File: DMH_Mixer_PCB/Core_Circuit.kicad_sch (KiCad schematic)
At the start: 28 parts, among them SW1 SW_SPDT_321, SW2 SW_SPDT_321, SW3 SW_SPDT_321, SW4 SW_SPDT_321, U1 TL074

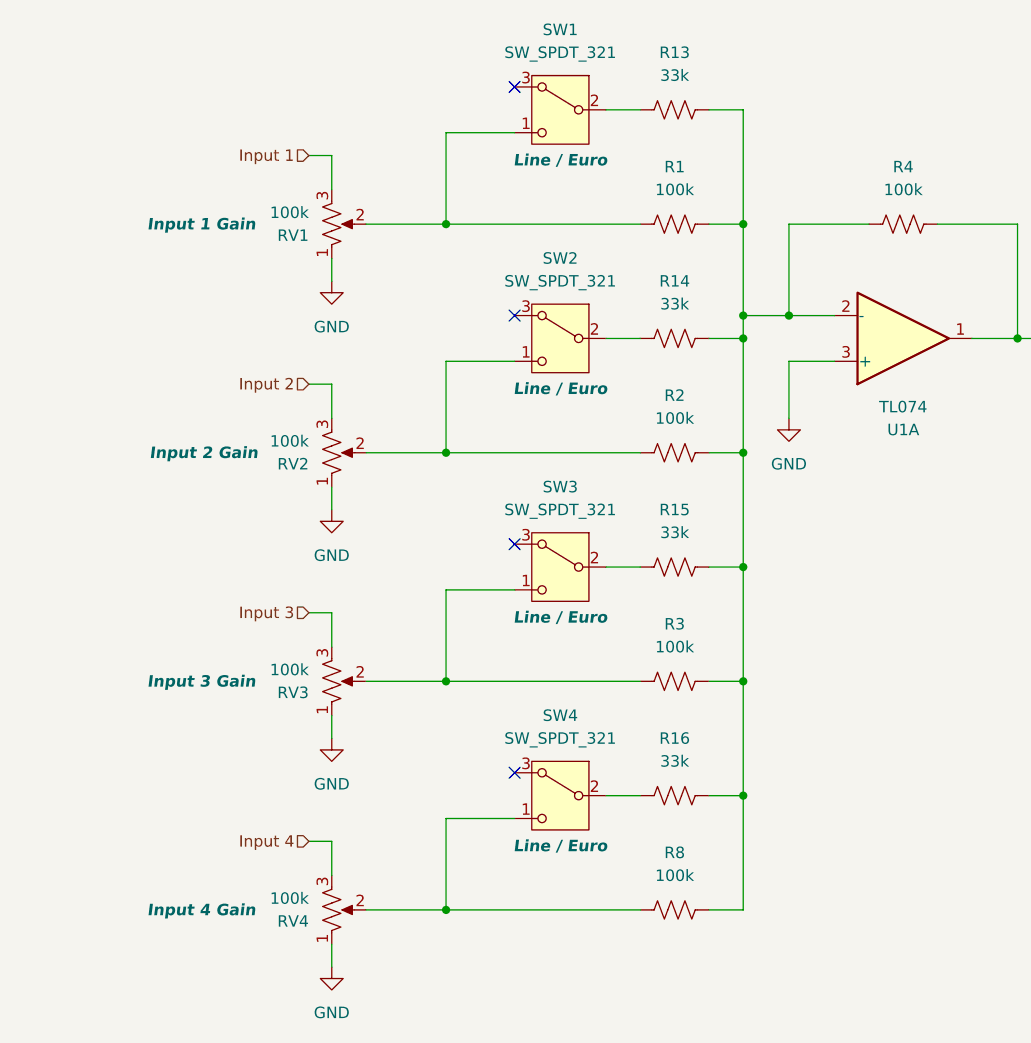
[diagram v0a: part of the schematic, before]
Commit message: Added AC coupling
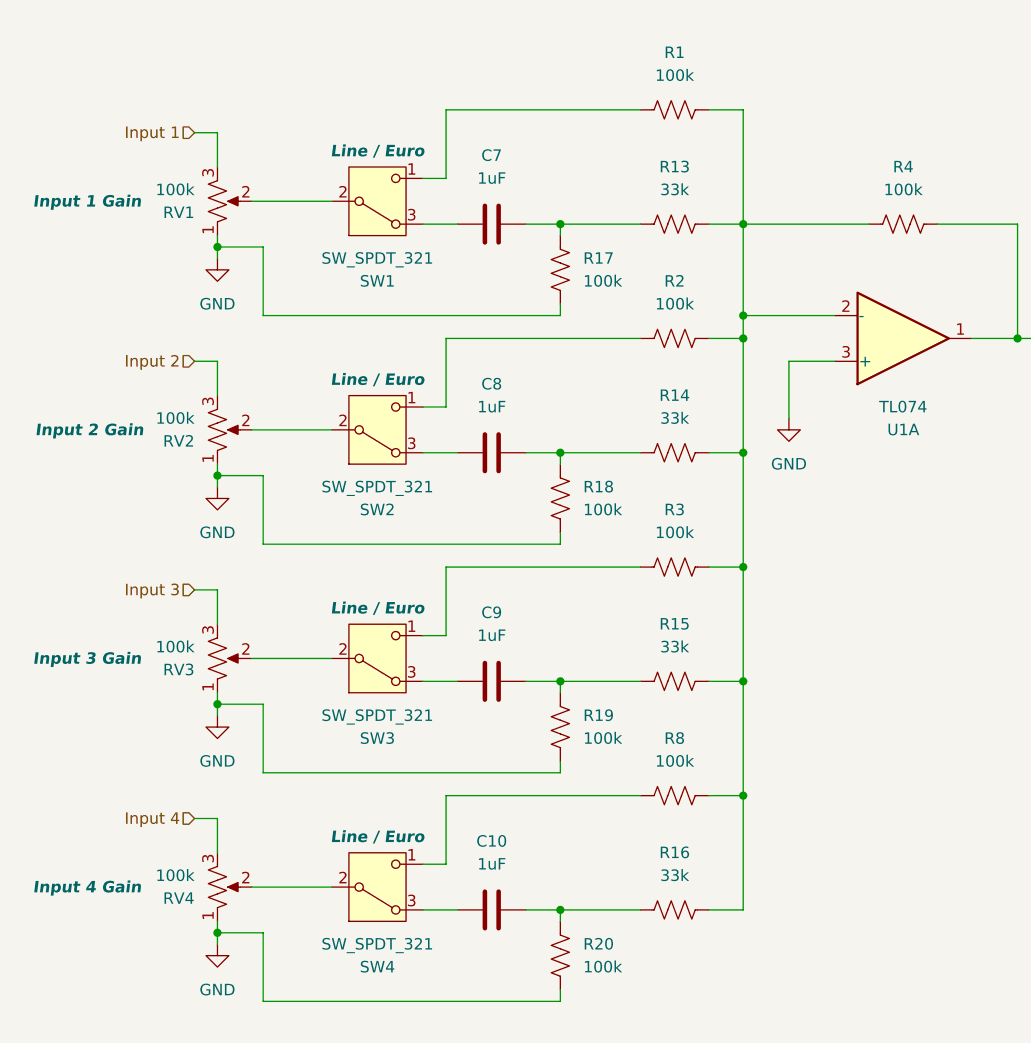
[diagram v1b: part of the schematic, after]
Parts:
- added C10, C7, C8, C9: 1uF, Capacitor_THT:C_Disc_D4.3mm_W1.9mm_P5.00mm, symbol Device:C
- added R17, R18, R19, R20: 100k, Resistor_THT:R_Axial_DIN0207_L6.3mm_D2.5mm_P7.62mm_Horizontal, symbol Device:R_US
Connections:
- net GND: now also R17.1, R18.1, R19.1, R20.1
- net at R14.1: now also C8.2, R18.2; no longer SW2.2 (B)
- net at R2.1, SW2.1 (C): no longer RV2.2
- net at R3.1, SW3.1 (C): no longer RV3.2
- net at R15.1: now also C9.2, R19.2; no longer SW3.2 (B)
- net at SW3.3 (A): now also C9.1
- net at R8.1, SW4.1 (C): no longer RV4.2
- net at R1.1, SW1.1 (C): no longer RV1.2
- net at SW2.3 (A): now also C8.1
- net at R13.1: now also C7.2, R17.2; no longer SW1.2 (B)
- net at R16.1: now also C10.2, R20.2; no longer SW4.2 (B)
- net at SW1.3 (A): now also C7.1
- net at SW4.3 (A): now also C10.1
- new net: RV3.2, SW3.2 (B)
- new net: RV1.2, SW1.2 (B)
- new net: RV2.2, SW2.2 (B)
- new net: RV4.2, SW4.2 (B)
- no-connect marks 4 -> 0
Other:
- moved on the sheet: R1, R13, R14, R15, R16, R2, R3, R8, RV1, RV2, RV3, RV4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

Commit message: Component placement done
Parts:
- R2: renamed from R13; value 33k -> 27k
- R4: renamed from R14; value 33k -> 27k
- R6: renamed from R15; value 33k -> 27k
- R8: renamed from R16; value 33k -> 27k
- renumbered R18 to R10, R19 to R11, R20 to R12, R4 to R13, R5 to R14, R6 to R15, R7 to R16, R9 to R17, R11 to R18, R10 to R19, R12 to R20, R2 to R3, R3 to R5, R8 to R7, R17 to R9
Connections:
- net at C7.1: now also SW1.1 (C); no longer SW1.3 (A)
- net at R3.1: now also SW2.3 (A); no longer SW2.1 (C)
- net at SW3.1 (C): now also C9.1; no longer R5.1
- net at SW3.3 (A): now also R5.1; no longer C9.1
- net at C8.1: now also SW2.1 (C); no longer SW2.3 (A)
- net at R7.1: now also SW4.3 (A); no longer SW4.1 (C)
- net at R1.1: now also SW1.3 (A); no longer SW1.1 (C)
- net at C10.1: now also SW4.1 (C); no longer SW4.3 (A)
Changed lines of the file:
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@@
 		(dnp no)
 		(fields_autoplaced yes)
-		(property "Reference" "R14"
+		(property "Reference" "R4"
 			(at 88.9 82.55 90)
 			(effects
@@
 			)
 		)
-		(property "Value" "33k"
+		(property "Value" "27k"
 			(at 88.9 85.09 90)
 			(effects
@@
 			(project "DMH_Mixer_PCB"
 				(path "/58f4306d-5387-4983-bb08-41a2313fd315/7ad2d702-dfb7-4d49-a82d-34430dd5948f"
-					(reference "R14")
+					(reference "R4")
 					(unit 1)
 				)
@@
 		(dnp no)
 		(fields_autoplaced yes)
-		(property "Reference" "R12"
+		(property "Reference" "R20"
 			(at 241.3 97.79 90)
 			(effects
@@
 			(project "DMH_Mixer_PCB"
 				(path "/58f4306d-5387-4983-bb08-41a2313fd315/7ad2d702-dfb7-4d49-a82d-34430dd5948f"
-					(reference "R12")
+					(reference "R20")
 					(unit 1)
 				)
@@
 		(dnp no)
 		(fields_autoplaced yes)
-		(property "Reference" "R19"
+		(property "Reference" "R11"
 			(at 78.74 118.1099 0)
 			(effects
@@
 			(project "DMH_Mixer_PCB"
 				(path "/58f4306d-5387-4983-bb08-41a2313fd315/7ad2d702-dfb7-4d49-a82d-34430dd5948f"
-					(reference "R19")
+					(reference "R11")
 					(unit 1)
 				)
@@
 		(dnp no)
 		(fields_autoplaced yes)
-		(property "Reference" "R9"
+		(property "Reference" "R17"
 			(at 171.45 95.25 90)
 			(effects
@@
 			(project "DMH_Mixer_PCB"
 				(path "/58f4306d-5387-4983-bb08-41a2313fd315/7ad2d702-dfb7-4d49-a82d-34430dd5948f"
-					(reference "R9")
+					(reference "R17")
 					(unit 1)
 				)
@@
 		(dnp no)
 		(fields_autoplaced yes)
-		(property "Reference" "R2"
+		(property "Reference" "R3"
 			(at 88.9 69.85 90)
 			(effects
@@
 			(project "DMH_Mixer_PCB"
 				(path "/58f4306d-5387-4983-bb08-41a2313fd315/7ad2d702-dfb7-4d49-a82d-34430dd5948f"
-					(reference "R2")
+					(reference "R3")
 					(unit 1)
 				)
@@
 		(lib_id "Switch:SW_SPDT_321")
 		(at 55.88 111.76 0)
-		(mirror x)
 		(unit 1)
 		(exclude_from_sim no)
@@
 		(dnp no)
 		(property "Reference" "SW3"
-			(at 55.88 120.65 0)
+			(at 55.88 102.87 0)
 			(effects
 				(font
@@
 		)
 		(property "Value" "SW_SPDT_321"
-			(at 55.88 118.11 0)
+			(at 55.88 105.41 0)
 			(effects
 				(font
@@
 		)
 		(property "Footprint" "SynthStuff:Toggle_Switch_THT"
-			(at 55.88 101.6 0)
+			(at 55.88 121.92 0)
 			(effects
 				(font
@@
 		)
 		(property "Datasheet" "~"
-			(at 55.88 104.14 0)
+			(at 55.88 119.38 0)
 			(effects
 				(font
@@
 		)
 		(property "Function" "Line / Euro"
-			(at 55.88 106.172 0)
+			(at 55.88 117.348 0)
 			(effects
 				(font
@@
 		(dnp no)
 		(fields_autoplaced yes)
-		(property "Reference" "R8"
+		(property "Reference" "R7"
 			(at 88.9 120.65 90)
 			(effects
@@
 			(project "DMH_Mixer_PCB"
 				(path "/58f4306d-5387-4983-bb08-41a2313fd315/7ad2d702-dfb7-4d49-a82d-34430dd5948f"
-					(reference "R8")
+					(reference "R7")
 					(unit 1)
 				)
@@
 		(dnp no)
 		(fields_autoplaced yes)
-		(property "Reference" "R17"
+		(property "Reference" "R9"
 			(at 78.74 67.3099 0)
 			(effects
@@
 			(project "DMH_Mixer_PCB"
 				(path "/58f4306d-5387-4983-bb08-41a2313fd315/7ad2d702-dfb7-4d49-a82d-34430dd5948f"
-					(reference "R17")
+					(reference "R9")
 					(unit 1)
 				)
@@
 		(dnp no)
 		(fields_autoplaced yes)
-		(property "Reference" "R20"
+		(property "Reference" "R12"
 			(at 78.74 143.5099 0)
 			(effects
@@
 			(project "DMH_Mixer_PCB"
 				(path "/58f4306d-5387-4983-bb08-41a2313fd315/7ad2d702-dfb7-4d49-a82d-34430dd5948f"
-					(reference "R20")
+					(reference "R12")
 					(unit 1)
 				)
@@
 		(dnp no)
 		(fields_autoplaced yes)
-		(property "Reference" "R3"
+		(property "Reference" "R5"
 			(at 88.9 95.25 90)
 			(effects
@@
 			(project "DMH_Mixer_PCB"
 				(path "/58f4306d-5387-4983-bb08-41a2313fd315/7ad2d702-dfb7-4d49-a82d-34430dd5948f"
-					(reference "R3")
+					(reference "R5")
 					(unit 1)
 				)
@@
 		(lib_id "Switch:SW_SPDT_321")
 		(at 55.88 86.36 0)
-		(mirror x)
 		(unit 1)
 		(exclude_from_sim no)
@@
 		(dnp no)
 		(property "Reference" "SW2"
-			(at 55.88 95.25 0)
+			(at 55.88 77.47 0)
 			(effects
 				(font
@@
 		)
 		(property "Value" "SW_SPDT_321"
-			(at 55.88 92.71 0)
+			(at 55.88 80.01 0)
 			(effects
 				(font
@@
 		)
 		(property "Footprint" "SynthStuff:Toggle_Switch_THT"
-			(at 55.88 76.2 0)
+			(at 55.88 96.52 0)
 			(effects
 				(font
@@
 		)
 		(property "Datasheet" "~"
-			(at 55.88 78.74 0)
+			(at 55.88 93.98 0)
 			(effects
 				(font
@@
 		)
 		(property "Function" "Line / Euro"
-			(at 55.88 80.772 0)
+			(at 55.88 91.948 0)
 			(effects
 				(font
@@
 		(dnp no)
 		(fields_autoplaced yes)
-		(property "Reference" "R7"
+		(property "Reference" "R16"
 			(at 215.9 74.93 90)
 			(effects
@@
 			(project "DMH_Mixer_PCB"
 				(path "/58f4306d-5387-4983-bb08-41a2313fd315/7ad2d702-dfb7-4d49-a82d-34430dd5948f"
-					(reference "R7")
+					(reference "R16")
 					(unit 1)
 				)
@@
 		(dnp no)
 		(fields_autoplaced yes)
-		(property "Reference" "R13"
+		(property "Reference" "R2"
 			(at 88.9 57.15 90)
 			(effects
@@
 			)
 		)
-		(property "Value" "33k"
+		(property "Value" "27k"
 			(at 88.9 59.69 90)
 			(effects
@@
 			(project "DMH_Mixer_PCB"
 				(path "/58f4306d-5387-4983-bb08-41a2313fd315/7ad2d702-dfb7-4d49-a82d-34430dd5948f"
-					(reference "R13")
+					(reference "R2")
 					(unit 1)
 				)
@@
 		(on_board yes)
 		(dnp no)
-		(property "Reference" "R10"
+		(property "Reference" "R19"
 			(at 215.9 120.65 90)
 			(effects
@@
 			(project "DMH_Mixer_PCB"
 				(path "/58f4306d-5387-4983-bb08-41a2313fd315/7ad2d702-dfb7-4d49-a82d-34430dd5948f"
-					(reference "R10")
+					(reference "R19")
 					(unit 1)
 				)
@@
 		(dnp no)
 		(fields_autoplaced yes)
-		(property "Reference" "R4"
+		(property "Reference" "R13"
 			(at 114.3 57.15 90)
 			(effects
@@
 			(project "DMH_Mixer_PCB"
 				(path "/58f4306d-5387-4983-bb08-41a2313fd315/7ad2d702-dfb7-4d49-a82d-34430dd5948f"
-					(reference "R4")
+					(reference "R13")
 					(unit 1)
 				)
@@
 		(dnp no)
 		(fields_autoplaced yes)
-		(property "Reference" "R15"
+		(property "Reference" "R6"
 			(at 88.9 107.95 90)
 			(effects
@@
 			)
 		)
-		(property "Value" "33k"
+		(property "Value" "27k"
 			(at 88.9 110.49 90)
 			(effects
@@
 			(project "DMH_Mixer_PCB"
 				(path "/58f4306d-5387-4983-bb08-41a2313fd315/7ad2d702-dfb7-4d49-a82d-34430dd5948f"
-					(reference "R15")
+					(reference "R6")
 					(unit 1)
 				)
@@
 		(dnp no)
 		(fields_autoplaced yes)
-		(property "Reference" "R16"
+		(property "Reference" "R8"
 			(at 88.9 133.35 90)
 			(effects
@@
 			)
 		)
-		(property "Value" "33k"
+		(property "Value" "27k"
 			(at 88.9 135.89 90)
 			(effects
@@
 			(project "DMH_Mixer_PCB"
 				(path "/58f4306d-5387-4983-bb08-41a2313fd315/7ad2d702-dfb7-4d49-a82d-34430dd5948f"
-					(reference "R16")
+					(reference "R8")
 					(unit 1)
 				)
@@
 		(dnp no)
 		(fields_autoplaced yes)
-		(property "Reference" "R18"
+		(property "Reference" "R10"
 			(at 78.74 92.7099 0)
 			(effects
@@
 			(project "DMH_Mixer_PCB"
 				(path "/58f4306d-5387-4983-bb08-41a2313fd315/7ad2d702-dfb7-4d49-a82d-34430dd5948f"
-					(reference "R18")
+					(reference "R10")
 					(unit 1)
 				)
@@
 		(lib_id "Switch:SW_SPDT_321")
 		(at 55.88 60.96 0)
-		(mirror x)
 		(unit 1)
 		(exclude_from_sim no)
@@
 		(dnp no)
 		(property "Reference" "SW1"
-			(at 55.88 69.85 0)
+			(at 55.88 52.07 0)
 			(effects
 				(font
@@
 		)
 		(property "Value" "SW_SPDT_321"
-			(at 55.88 67.31 0)
+			(at 55.88 54.61 0)
 			(effects
 				(font
@@
 		)
 		(property "Footprint" "SynthStuff:Toggle_Switch_THT"
-			(at 55.88 50.8 0)
+			(at 55.88 71.12 0)
 			(effects
 				(font
@@
 		)
 		(property "Datasheet" "~"
-			(at 55.88 53.34 0)
+			(at 55.88 68.58 0)
 			(effects
 				(font
@@
 		)
 		(property "Function" "Line / Euro"
-			(at 55.88 55.372 0)
+			(at 55.88 66.548 0)
 			(effects
 				(font
@@
 		(on_board yes)
 		(dnp no)
-		(property "Reference" "R11"
+		(property "Reference" "R18"
 			(at 200.66 119.3799 0)
 			(effects
@@
 			(project "DMH_Mixer_PCB"
 				(path "/58f4306d-5387-4983-bb08-41a2313fd315/7ad2d702-dfb7-4d49-a82d-34430dd5948f"
-					(reference "R11")
+					(reference "R18")
 					(unit 1)
 				)
@@
 		(dnp no)
 		(fields_autoplaced yes)
-		(property "Reference" "R6"
+		(property "Reference" "R15"
 			(at 152.4 57.15 90)
 			(effects
@@
 			(project "DMH_Mixer_PCB"
 				(path "/58f4306d-5387-4983-bb08-41a2313fd315/7ad2d702-dfb7-4d49-a82d-34430dd5948f"
-					(reference "R6")
+					(reference "R15")
 					(unit 1)
 				)
@@
 		(dnp no)
 		(fields_autoplaced yes)
-		(property "Reference" "R5"
+		(property "Reference" "R14"
 			(at 133.35 69.85 90)
 			(effects
@@
 			(project "DMH_Mixer_PCB"
 				(path "/58f4306d-5387-4983-bb08-41a2313fd315/7ad2d702-dfb7-4d49-a82d-34430dd5948f"
-					(reference "R5")
+					(reference "R14")
 					(unit 1)
 				)
@@
 		(lib_id "Switch:SW_SPDT_321")
 		(at 55.88 137.16 0)
-		(mirror x)
 		(unit 1)
 		(exclude_from_sim no)
@@
 		(dnp no)
 		(property "Reference" "SW4"
-			(at 55.88 146.05 0)
+			(at 55.88 128.27 0)
 			(effects
 				(font
@@
 		)
 		(property "Value" "SW_SPDT_321"
-			(at 55.88 143.51 0)
+			(at 55.88 130.81 0)
 			(effects
 				(font
@@
 		)
 		(property "Footprint" "SynthStuff:Toggle_Switch_THT"
-			(at 55.88 127 0)
+			(at 55.88 147.32 0)
 			(effects
 				(font
@@
 		)
 		(property "Datasheet" "~"
-			(at 55.88 129.54 0)
+			(at 55.88 144.78 0)
 			(effects
 				(font
@@
 		)
 		(property "Function" "Line / Euro"
-			(at 55.88 131.572 0)
+			(at 55.88 142.748 0)
 			(effects
 				(font

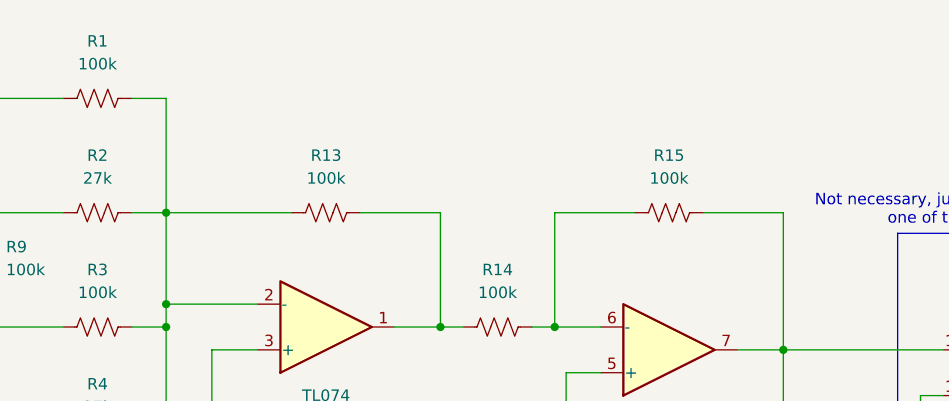
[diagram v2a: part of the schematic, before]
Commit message: ReRouted PCB
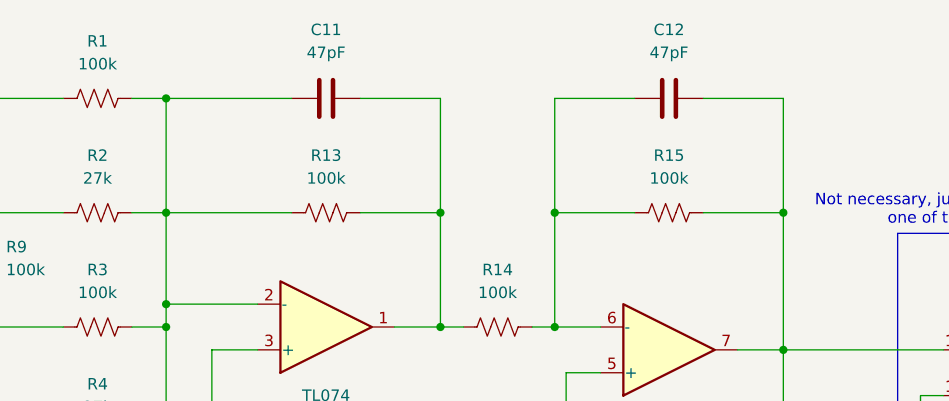
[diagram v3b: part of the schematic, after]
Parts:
- added C11, C12: 47pF, Capacitor_THT:C_Disc_D3.0mm_W2.0mm_P2.50mm, symbol Device:C
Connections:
- net at R1.2, R13.1, R2.2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: now also C11.1
- net at R15.2, R17.1, U1.12 (+)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: now also C12.2
- net at R13.2, R14.1, U1.1: now also C11.2
- net at R14.2, R15.1, U1.6 (-): now also C12.1
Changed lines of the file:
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@@
 	)
 	(junction
+		(at 165.1 63.5)
+		(diameter 0)
+		(color 0 0 0 0)
+	)
+	(junction
 		(at 38.1 142.24)
 		(diameter 0)
@@
 	)
 	(junction
+		(at 139.7 63.5)
+		(diameter 0)
+		(color 0 0 0 0)
+	)
+	(junction
 		(at 96.52 76.2)
 		(diameter 0)
@@
 	)
 	(junction
+		(at 127 63.5)
+		(diameter 0)
+		(color 0 0 0 0)
+	)
+	(junction
+		(at 96.52 50.8)
+		(diameter 0)
+		(color 0 0 0 0)
+	)
+	(junction
 		(at 190.5 101.6)
 		(diameter 0)
@@
 	(wire
 		(pts
+			(xy 148.59 50.8) (xy 139.7 50.8)
+		)
+		(stroke
+			(width 0)
+			(type default)
+		)
+	)
+	(wire
+		(pts
 			(xy 38.1 142.24) (xy 38.1 143.51)
 		)
@@
 	(wire
 		(pts
+			(xy 96.52 50.8) (xy 110.49 50.8)
+		)
+		(stroke
+			(width 0)
+			(type default)
+		)
+	)
+	(wire
+		(pts
 			(xy 223.52 104.14) (xy 228.6 104.14)
 		)
@@
 	(wire
 		(pts
+			(xy 139.7 50.8) (xy 139.7 63.5)
+		)
+		(stroke
+			(width 0)
+			(type default)
+		)
+	)
+	(wire
+		(pts
 			(xy 190.5 101.6) (xy 208.28 101.6)
 		)
@@
 	(wire
 		(pts
+			(xy 118.11 50.8) (xy 127 50.8)
+		)
+		(stroke
+			(width 0)
+			(type default)
+		)
+	)
+	(wire
+		(pts
 			(xy 76.2 73.66) (xy 76.2 72.39)
 		)
@@
 	(wire
 		(pts
+			(xy 165.1 50.8) (xy 165.1 63.5)
+		)
+		(stroke
+			(width 0)
+			(type default)
+		)
+	)
+	(wire
+		(pts
 			(xy 76.2 73.66) (xy 43.18 73.66)
 		)
@@
 	(wire
 		(pts
+			(xy 156.21 50.8) (xy 165.1 50.8)
+		)
+		(stroke
+			(width 0)
+			(type default)
+		)
+	)
+	(wire
+		(pts
 			(xy 63.5 50.8) (xy 85.09 50.8)
 		)
@@
 	(wire
 		(pts
+			(xy 127 50.8) (xy 127 63.5)
+		)
+		(stroke
+			(width 0)
+			(type default)
+		)
+	)
+	(wire
+		(pts
 			(xy 41.91 60.96) (xy 50.8 60.96)
 		)
@@
 	)
 	(symbol
+		(lib_id "Device:C")
+		(at 114.3 50.8 90)
+		(unit 1)
+		(exclude_from_sim no)
+		(in_bom yes)
+		(on_board yes)
+		(dnp no)
+		(fields_autoplaced yes)
+		(property "Reference" "C11"
+			(at 114.3 43.18 90)
+			(effects
+				(font
+					(size 1.27 1.27)
+				)
+			)
+		)
+		(property "Value" "47pF"
+			(at 114.3 45.72 90)
+			(effects
+				(font
+					(size 1.27 1.27)
+				)
+			)
+		)
+		(property "Footprint" "Capacitor_THT:C_Disc_D3.0mm_W2.0mm_P2.50mm"
+			(at 118.11 49.8348 0)
+			(effects
+				(font
+					(size 1.27 1.27)
+				)
+				(hide yes)
+			)
+		)
+		(property "Datasheet" "~"
+			(at 114.3 50.8 0)
+			(effects
+				(font
+					(size 1.27 1.27)
+				)
+				(hide yes)
+			)
+		)
+		(property "Description" "Unpolarized capacitor"
+			(at 114.3 50.8 0)
+			(effects
+				(font
+					(size 1.27 1.27)
+				)
+				(hide yes)
+			)
+		)
+		(property "Function" ""
+			(at 114.3 50.8 0)
+			(effects
+				(font
+					(size 1.27 1.27)
+				)
+			)
+		)
+		(pin "2"
+		)
+		(pin "1"
+		)
+		(instances
+			(project ""
+				(path "/58f4306d-5387-4983-bb08-41a2313fd315/7ad2d702-dfb7-4d49-a82d-34430dd5948f"
+					(reference "C11")
+					(unit 1)
+				)
+			)
+		)
+	)
+	(symbol
 		(lib_id "Device:R_Potentiometer_US")
 		(at 38.1 137.16 0)
@@
 					(unit 1)
 				)
+			)
+		)
+	)
+	(symbol
+		(lib_id "Device:C")
+		(at 152.4 50.8 90)
+		(unit 1)
+		(exclude_from_sim no)
+		(in_bom yes)
+		(on_board yes)
+		(dnp no)
+		(fields_autoplaced yes)
+		(property "Reference" "C12"
+			(at 152.4 43.18 90)
+			(effects
+				(font
+					(size 1.27 1.27)
+				)
+			)
+		)
+		(property "Value" "47pF"
+			(at 152.4 45.72 90)
+			(effects
+				(font
+					(size 1.27 1.27)
+				)
+			)
+		)
+		(property "Footprint" "Capacitor_THT:C_Disc_D3.0mm_W2.0mm_P2.50mm"
+			(at 156.21 49.8348 0)
+			(effects
+				(font
+					(size 1.27 1.27)
+				)
+				(hide yes)
+			)
+		)
+		(property "Datasheet" "~"
+			(at 152.4 50.8 0)
+			(effects
+				(font
+					(size 1.27 1.27)
+				)
+				(hide yes)
+			)
+		)
+		(property "Description" "Unpolarized capacitor"
+			(at 152.4 50.8 0)
+			(effects
+				(font
+					(size 1.27 1.27)
+				)
+				(hide yes)
+			)
+		)
+		(property "Function" ""
+			(at 152.4 50.8 0)
+			(effects
+				(font
+					(size 1.27 1.27)
+				)
+			)
+		)
+		(pin "2"
+		)
+		(pin "1"
+		)
+		(instances
+			(project ""
+				(path "/58f4306d-5387-4983-bb08-41a2313fd315/7ad2d702-dfb7-4d49-a82d-34430dd5948f"
+					(reference "C12")
+					(unit 1)
+				)
